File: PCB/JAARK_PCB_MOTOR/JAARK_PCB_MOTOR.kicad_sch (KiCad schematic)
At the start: 32 parts, among them IC1 TPS564242DRLR, IC10 DRV8231DDAR, IC9 DRV8231DDAR, J1 Battery Terminal, J2 Morpho_x2_SSW-119-01-T-D, J3 HC-05, Q1 SSM3J334RLF, Q3 BC237B, U1 4A

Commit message: Motor PCB finished?
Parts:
- added J4: Metal Detector, JAARK_lib:1984617, symbol SSys_Parts:1984617
- R2: footprint JAARK_lib:RESC2012X60N -> JAARK_lib:RESC2012X65N; Height 0.6 -> 0.65; Manufacturer_Name KEMET -> TE Connectivity; Manufacturer_Part_Number RC0805FR-0730K1L -> CRG0805F30K; Mouser Part Number 603-RC0805FR-0730K1L -> 279-CRG0805F30K; Mouser Price/Stock https://www.mouser.com/Search/Refine.aspx?Keyword=603-RC080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 -> https://www.mouser.co.uk/ProductDetail/TE-Connectivity-Hols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
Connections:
- net +12V: now also J4.2
- net GND: now also J4.1
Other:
- note added: "Bluetooth Module"
- moved on the sheet: J2A, J2B, J3, Q3, R6

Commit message: added test points
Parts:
- removed R5: 20kR, JAARK_lib:RESC2012X50N, symbol Device:R_Small_US
- added C8, C9: 0.1uF, JAARK_lib:C0805, symbol Device:C_Small
- added TP1: 12V, TestPoint:TestPoint_Pad_1.5x1.5mm, symbol Connector:TestPoint
- added TP2: 5V, TestPoint:TestPoint_Pad_1.5x1.5mm, symbol Connector:TestPoint
- added TP3: 3.3V, TestPoint:TestPoint_Pad_1.5x1.5mm, symbol Connector:TestPoint
- added TP4: GND, TestPoint:TestPoint_Pad_1.5x1.5mm, symbol Connector:TestPoint
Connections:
- net +12V: now also TP1.1
- net +3V3: now also C9.2, TP3.1
- net +5V: now also C8.2, TP2.1
- net GND: now also C7.2 (-), C8.1, C9.1, TP4.1

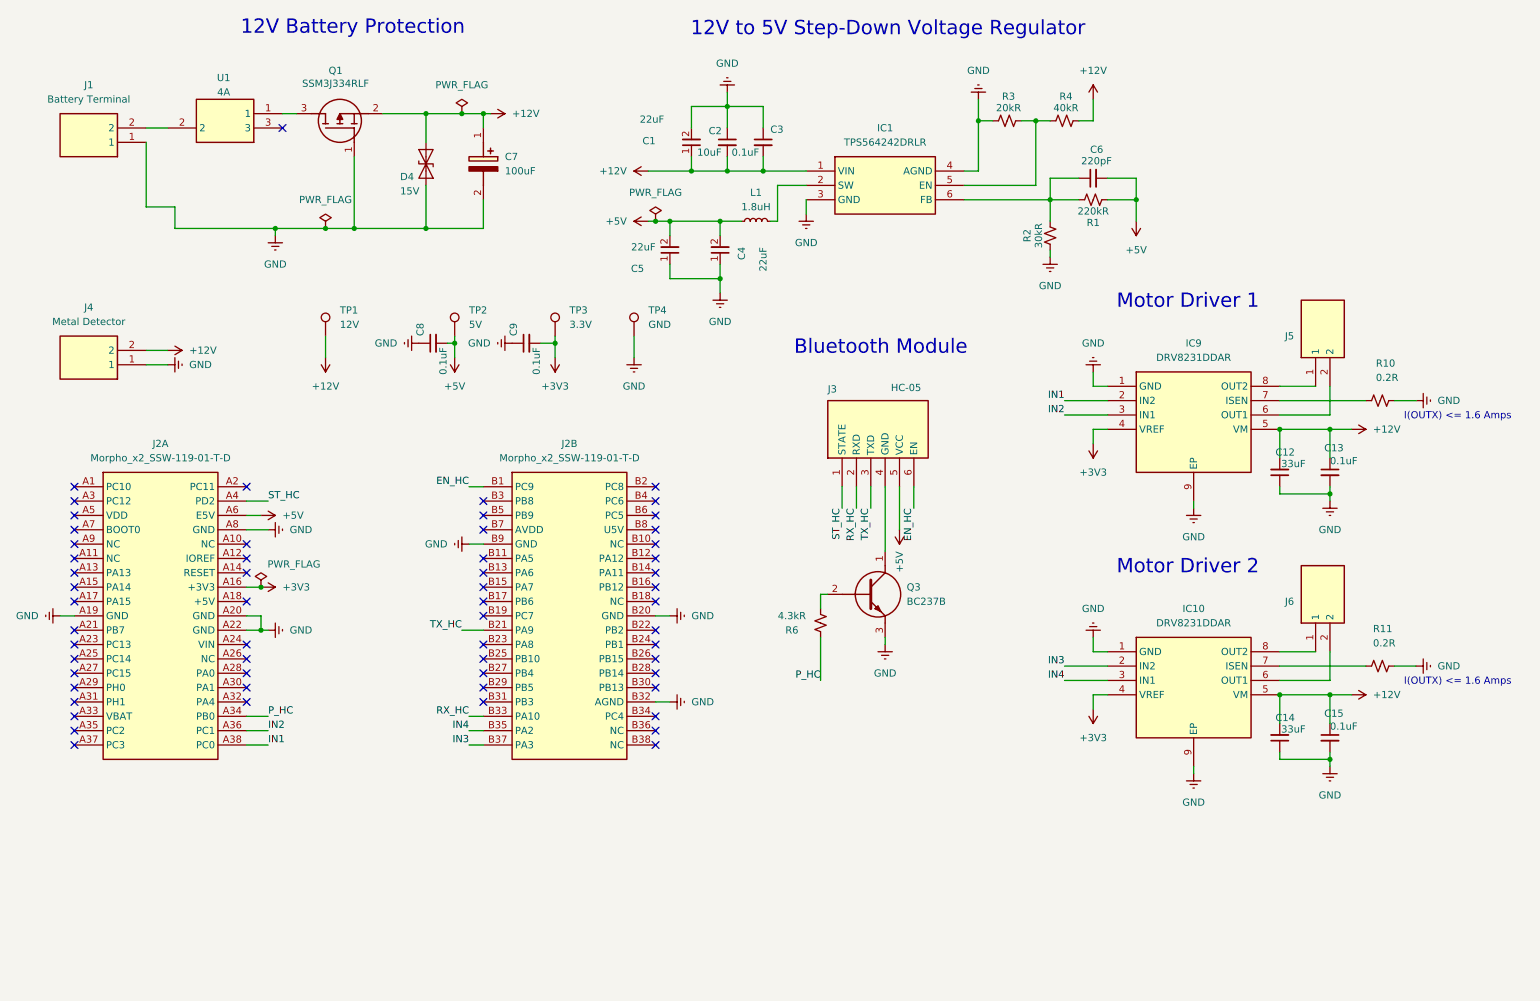
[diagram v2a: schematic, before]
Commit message: JLCPCB compatibility
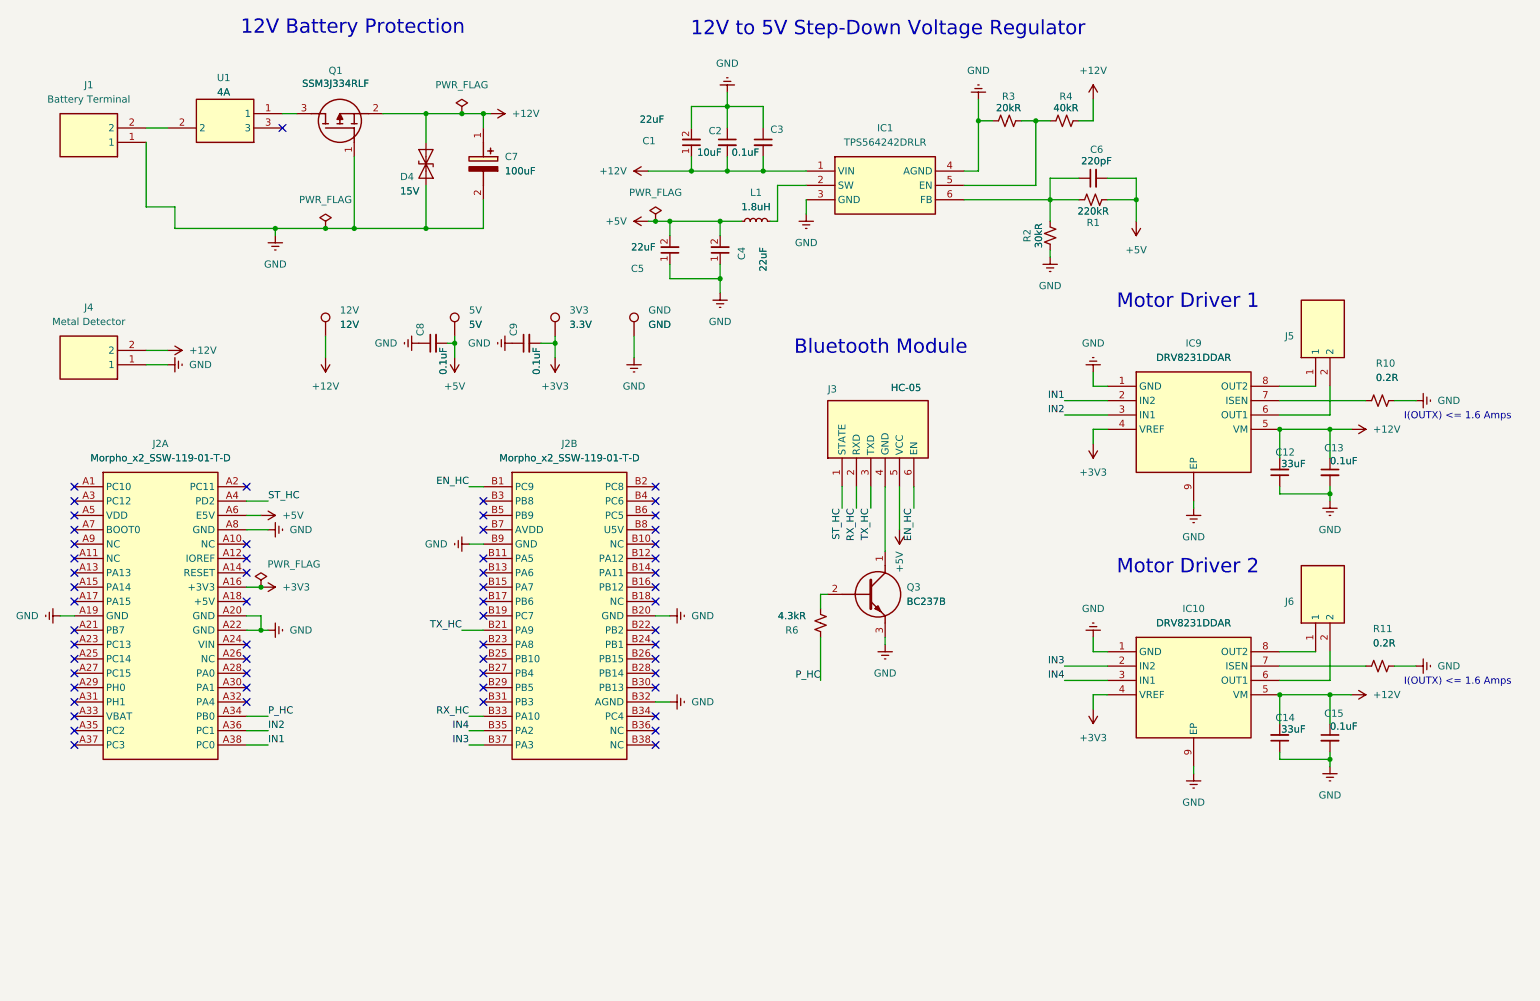
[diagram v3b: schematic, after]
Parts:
- 12V: renamed from TP1; now left out of the parts list
- 3V3: renamed from TP3; now left out of the parts list
- 5V: renamed from TP2; now left out of the parts list
- GND: renamed from TP4; now left out of the parts list
- J2: now in the parts list
- Q1: Arrow Part Number SSM3J334R,LF -> (none); Arrow Price/Stock https://www.arrow.com/en/products/ssm3j334rlf/toshiba?regio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 -> (none); Mouser Part Number 757-SSM3J334RLF -> (none); Mouser Price/Stock https://www.mouser.co.uk/ProductDetail/Toshiba/SSM3J334RLF?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 -> (none)

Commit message: Final prototype of PCB
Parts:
- removed U1: 4A, JAARK_lib:3586TR, symbol JAARK_lib:3586TR
- added J7: Metal Detector, JAARK_lib:1984617, symbol SSys_Parts:1984617
- added U1: 3568, 3568, symbol JAARK_lib:3568
- renumbered 12V to 12V1, 5V to 5V1, GND to GND1
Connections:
- net +12V: now also R3.1; no longer R4.1
- net +5V: now also J7.2
- net GND: now also R4.2, J7.1; no longer R3.2
- net IN3: now also IC10.3 (IN1); no longer IC10.2 (IN2)
- net IN4: now also IC10.2 (IN2); no longer IC10.3 (IN1)
- net at J1.2: now also U1.1, U1.2
- net at Q1.3 (D): now also U1.3, U1.4
- new net: IC1.5 (EN), R3.2, R4.1
- no-connect marks 59 -> 58
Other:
- moved on the sheet: C7, D4, GND1, J4, Q3, R3, R4

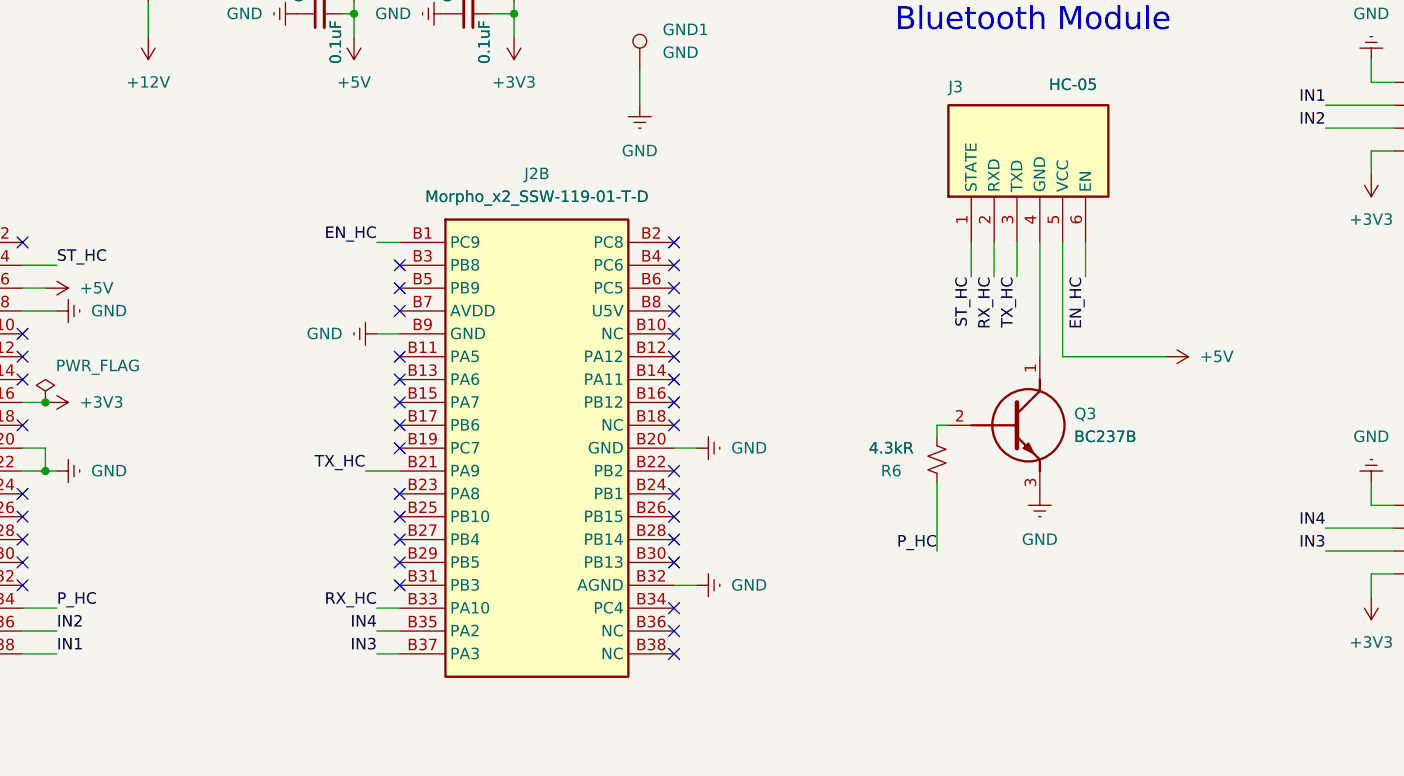
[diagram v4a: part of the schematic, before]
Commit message: Ultrasonic sensor code working on the STM32 with custom LCD driver
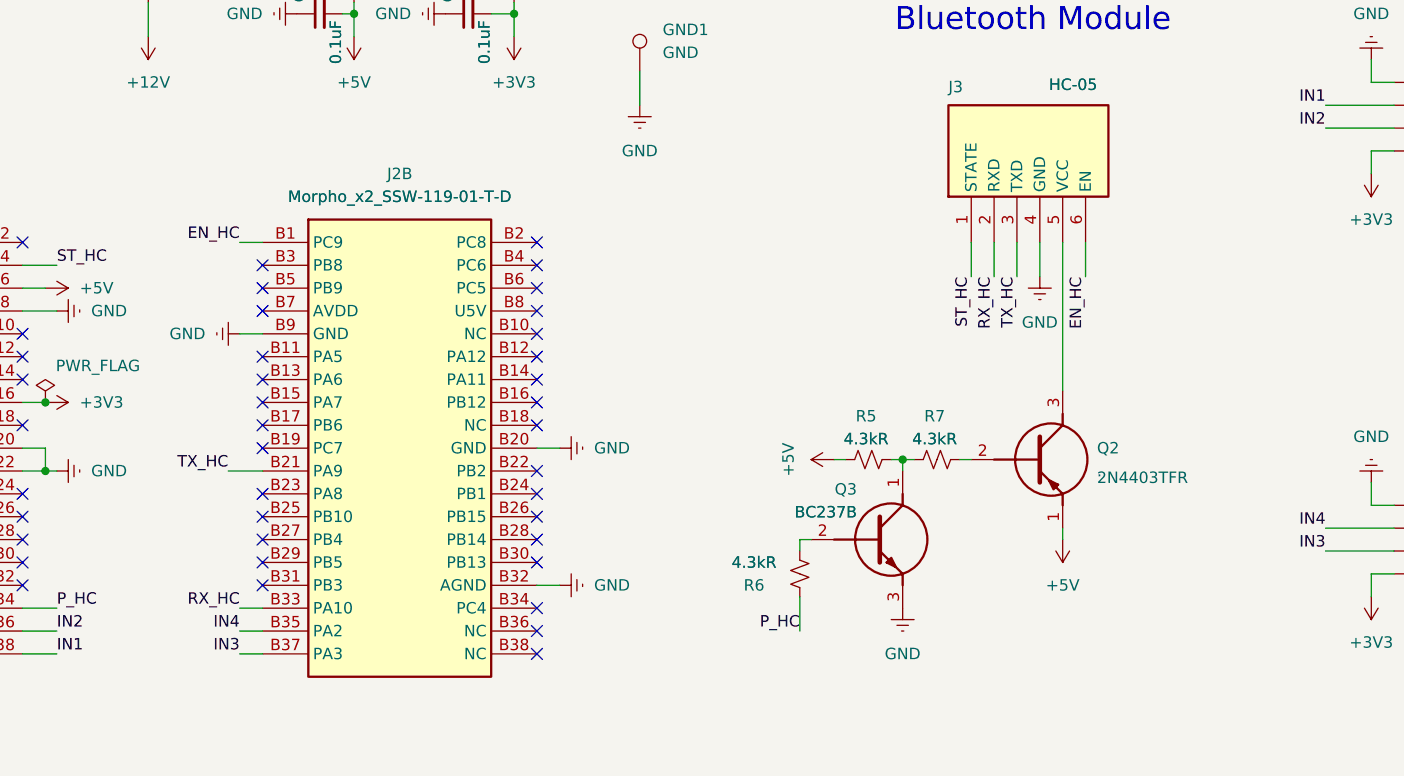
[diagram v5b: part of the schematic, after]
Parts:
- added Q2: 2N4403TFR, BC33740TA, symbol JAARK_lib:2N4403TFR
- added R5, R7: 4.3kR, Resistor_THT:R_Axial_DIN0207_L6.3mm_D2.5mm_P10.16mm_Horizontal, symbol Device:R_Small_US
- D4: Manufacturer Name (none) -> Littelfuse; Manufacturer Part Number (none) -> SMF12CA
- Q3: Manufacturer Part Number (none) -> BC237B; now left out of the parts list
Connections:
- net +5V: now also Q2.1 (E), R5.1; no longer J3.5 (VCC)
- net GND: now also J3.4 (GND)
- net at Q3.1 (C): now also R5.2, R7.1; no longer J3.4 (GND)
- new net: Q2.2 (B), R7.2
- new net: J3.5 (VCC), Q2.3 (C)
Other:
- moved on the sheet: J2B, Q3, R6
